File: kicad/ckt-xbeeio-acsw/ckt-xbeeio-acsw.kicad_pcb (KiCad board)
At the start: 2 copper layers, 95.2 x 102.9 mm, 47 parts, among them J1 Screw_Terminal_01x02, J2 Screw_Terminal_01x02, J3 Screw_Terminal_01x02, J4 Screw_Terminal_01x02, J5 Conn_AVR_TagConnect_TC2030, K1 ADJH23xxx, K2 ADJH23xxx, K3 ADJH23xxx, U1 RAC03E-12SK_277, U2 AP63203WU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

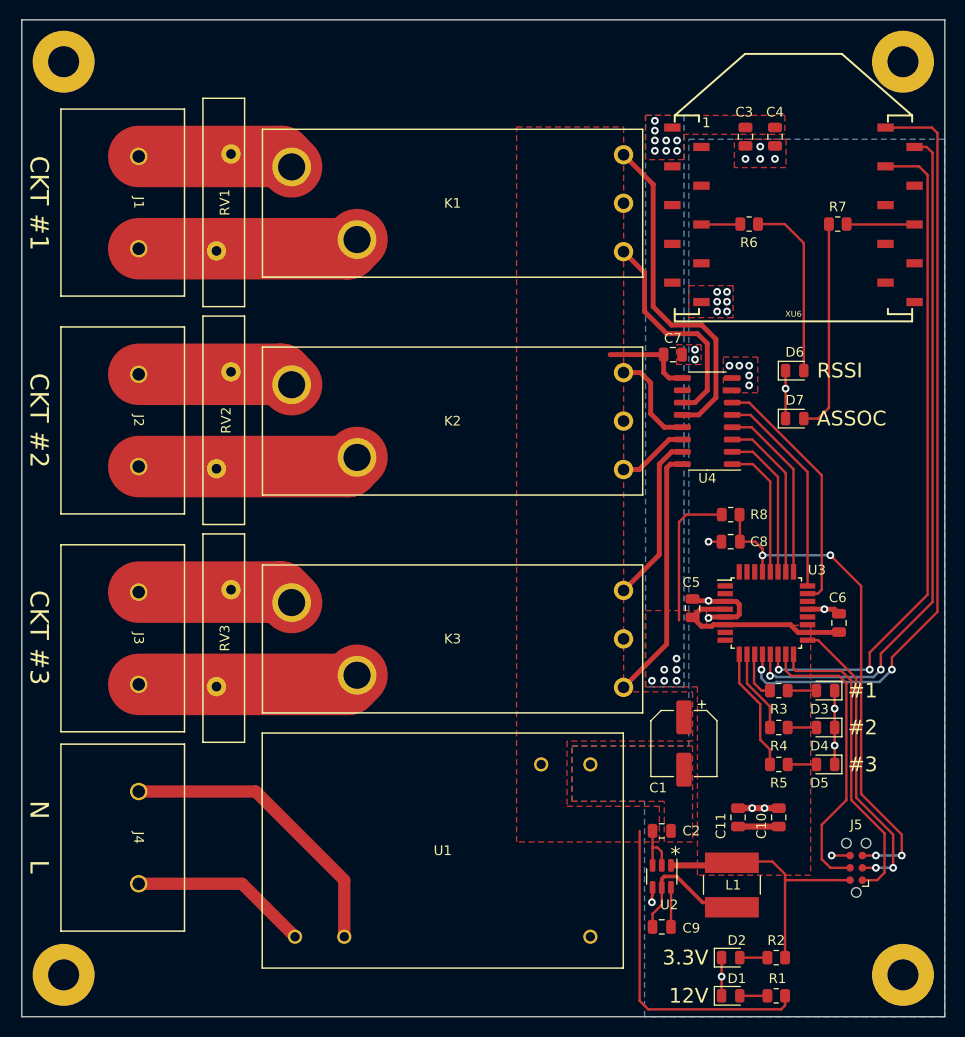
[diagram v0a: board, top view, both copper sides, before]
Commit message: Improved metalization, added text
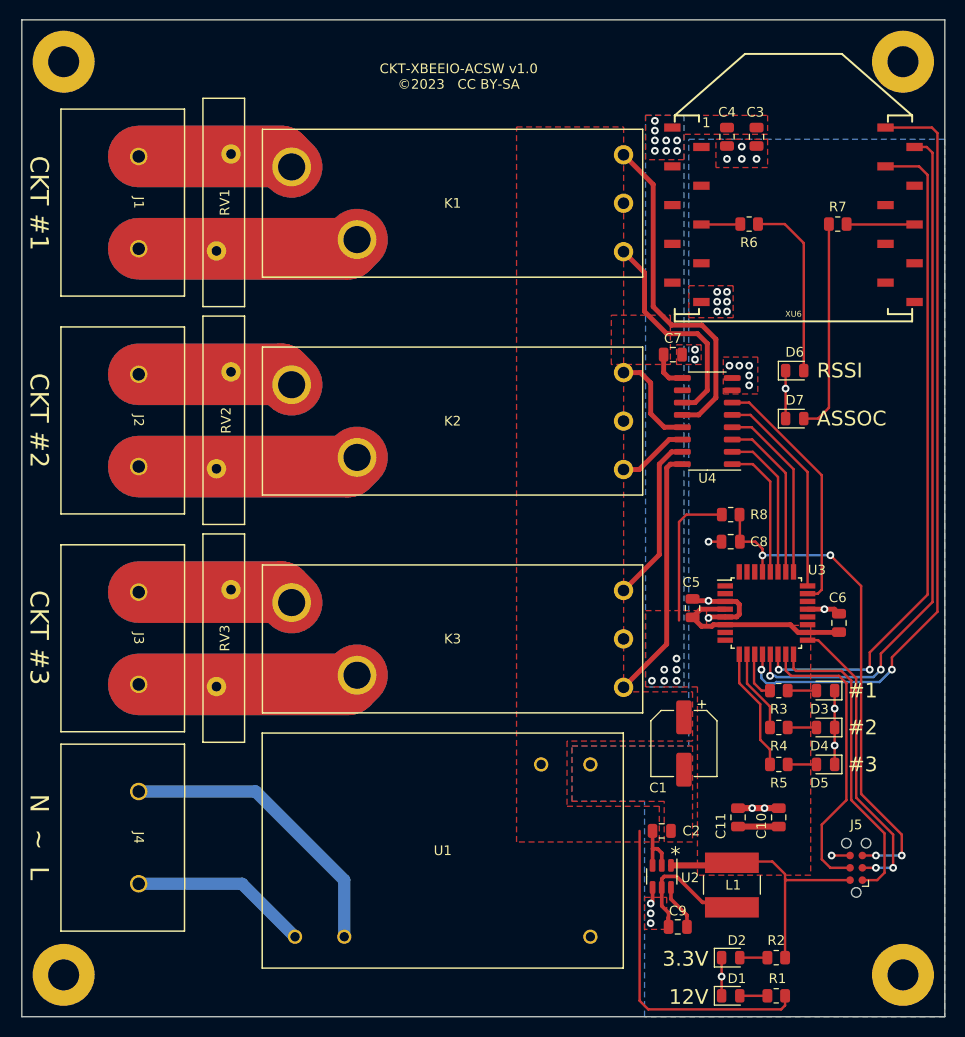
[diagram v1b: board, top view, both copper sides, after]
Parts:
- moved C4 4.95 mm to (104.5, 74.5)
- moved C9 1.65 mm to (99.4, 156.1)
- moved C3 1.14 mm to (107.6, 74.5)
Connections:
- U4 pad 7: unconnected-(U4-Pad7) -> GND
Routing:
- net Net-(J2-Pad2): track 22.9 -> 45.8 mm
- net Net-(J1-Pad2): track 22.9 -> 45.8 mm
- net Net-(J3-Pad2): track 22.9 -> 45.8 mm
- net Net-(J3-Pad1): track 16.2 -> 32.5 mm
- net Net-(J2-Pad1): track 16.2 -> 32.5 mm
- net Net-(J1-Pad1): track 16.2 -> 32.5 mm
- net +12V: track 49.7 -> 44.0 mm
- net Net-(C9-Pad2): track 4.07 -> 4.75 mm
- net GND: track 38.2 -> 38.4 mm, vias 29 -> 31
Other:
- board text added: "CKT-XBEEIO-ACSW v1.0 ©2023 CC BY-SA"
- board text added: "N ~ L"
- board text removed: "N L"

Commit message: Small improvements
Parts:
- moved C11 5.83 mm to (111.4, 143.6), turned to 0 degrees
- moved C10 2.41 mm to (111.4, 146.7), turned to 0 degrees
- moved C4 0.25 mm to (104.8, 74.5)
- moved C3 0.25 mm to (107.8, 74.5)
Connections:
- net Net-(C8-Pad1) renamed /~{RESET}
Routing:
- net +3.3V: track 66.1 -> 57.2 mm
- net GND: track 38.4 -> 32.5 mm, vias 31 -> 52

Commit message: Changed soldermask clearance to 3mil
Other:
- rule pad_to_mask_clearance: 0 -> 0.0762
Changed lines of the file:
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@@
       (dielectric_constraints no)
     )
-    (pad_to_mask_clearance 0)
+    (pad_to_mask_clearance 0.0762)
     (pcbplotparams
       (layerselection 0x00010fc_ffffffff)
